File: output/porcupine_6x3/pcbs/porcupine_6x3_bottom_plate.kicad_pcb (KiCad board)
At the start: 2 copper layers, 166.4 x 113.7 mm, 0 parts

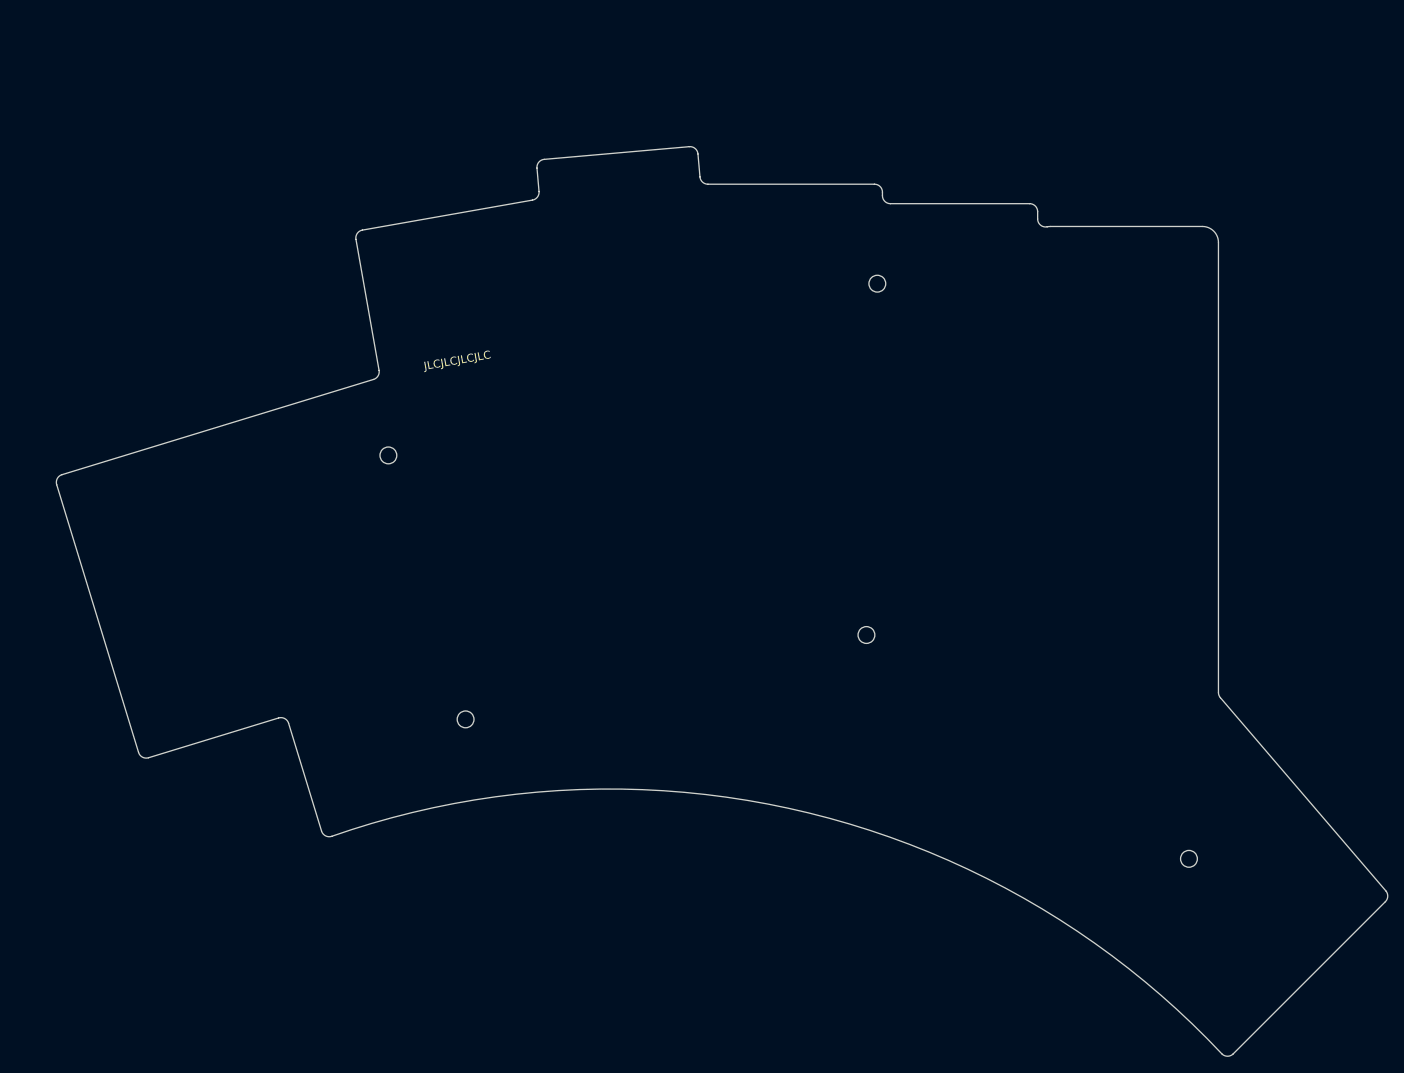
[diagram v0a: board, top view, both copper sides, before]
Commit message: Update 6x3 variant
* Removed unnecessary P19 via
* Fix outer column stagger
* Fix P19 matrix ring bottom via
* Resized GND zones
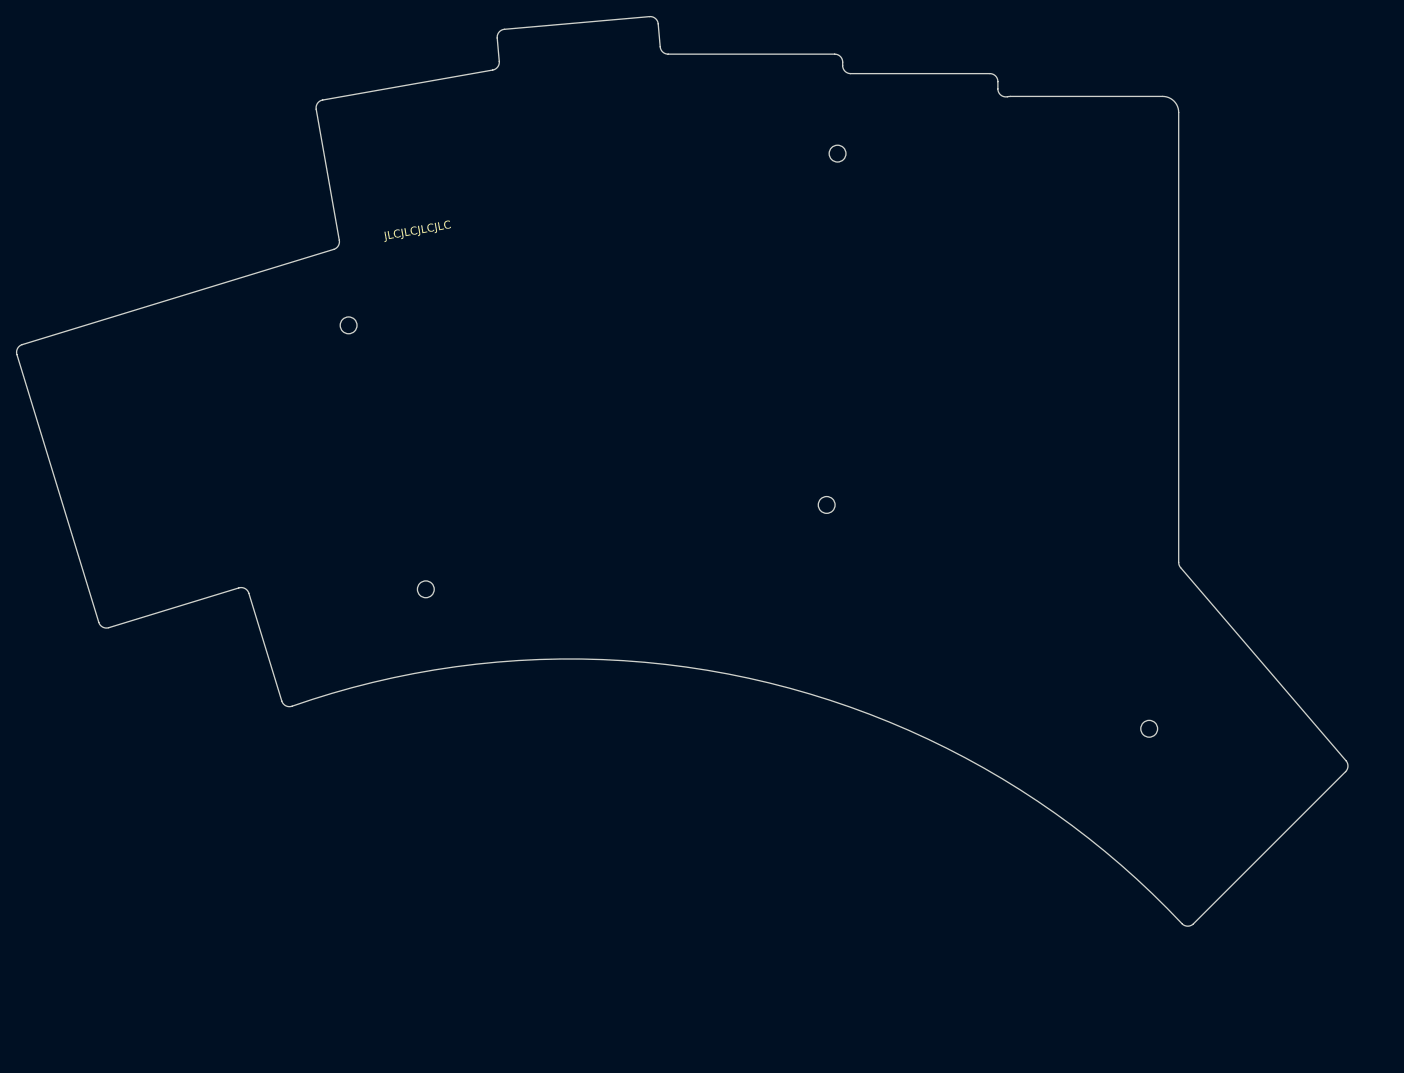
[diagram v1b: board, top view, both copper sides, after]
